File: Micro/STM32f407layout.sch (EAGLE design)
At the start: 44 parts, among them Q1 ASF, T3 FDN340P, T4 AP1117_LIN_REG

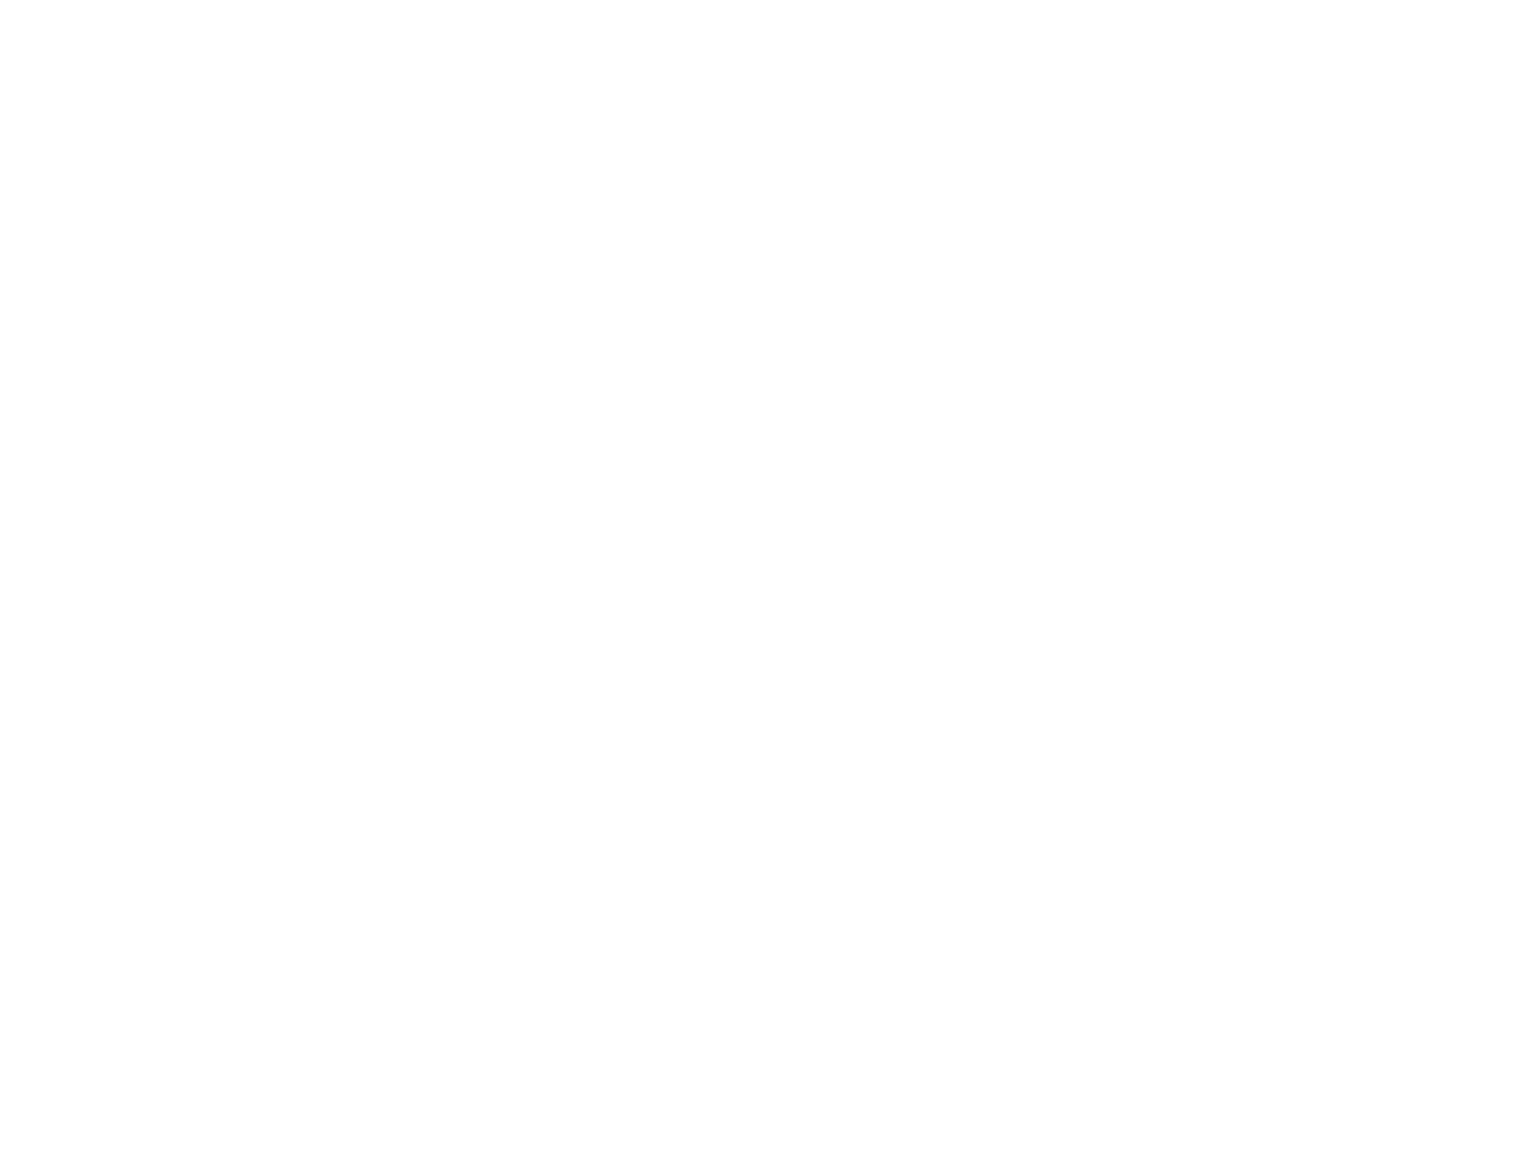
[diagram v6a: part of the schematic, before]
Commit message: Ethernet Addition
I added the ethernet chip and added essential routes, need to do
tolerance checks
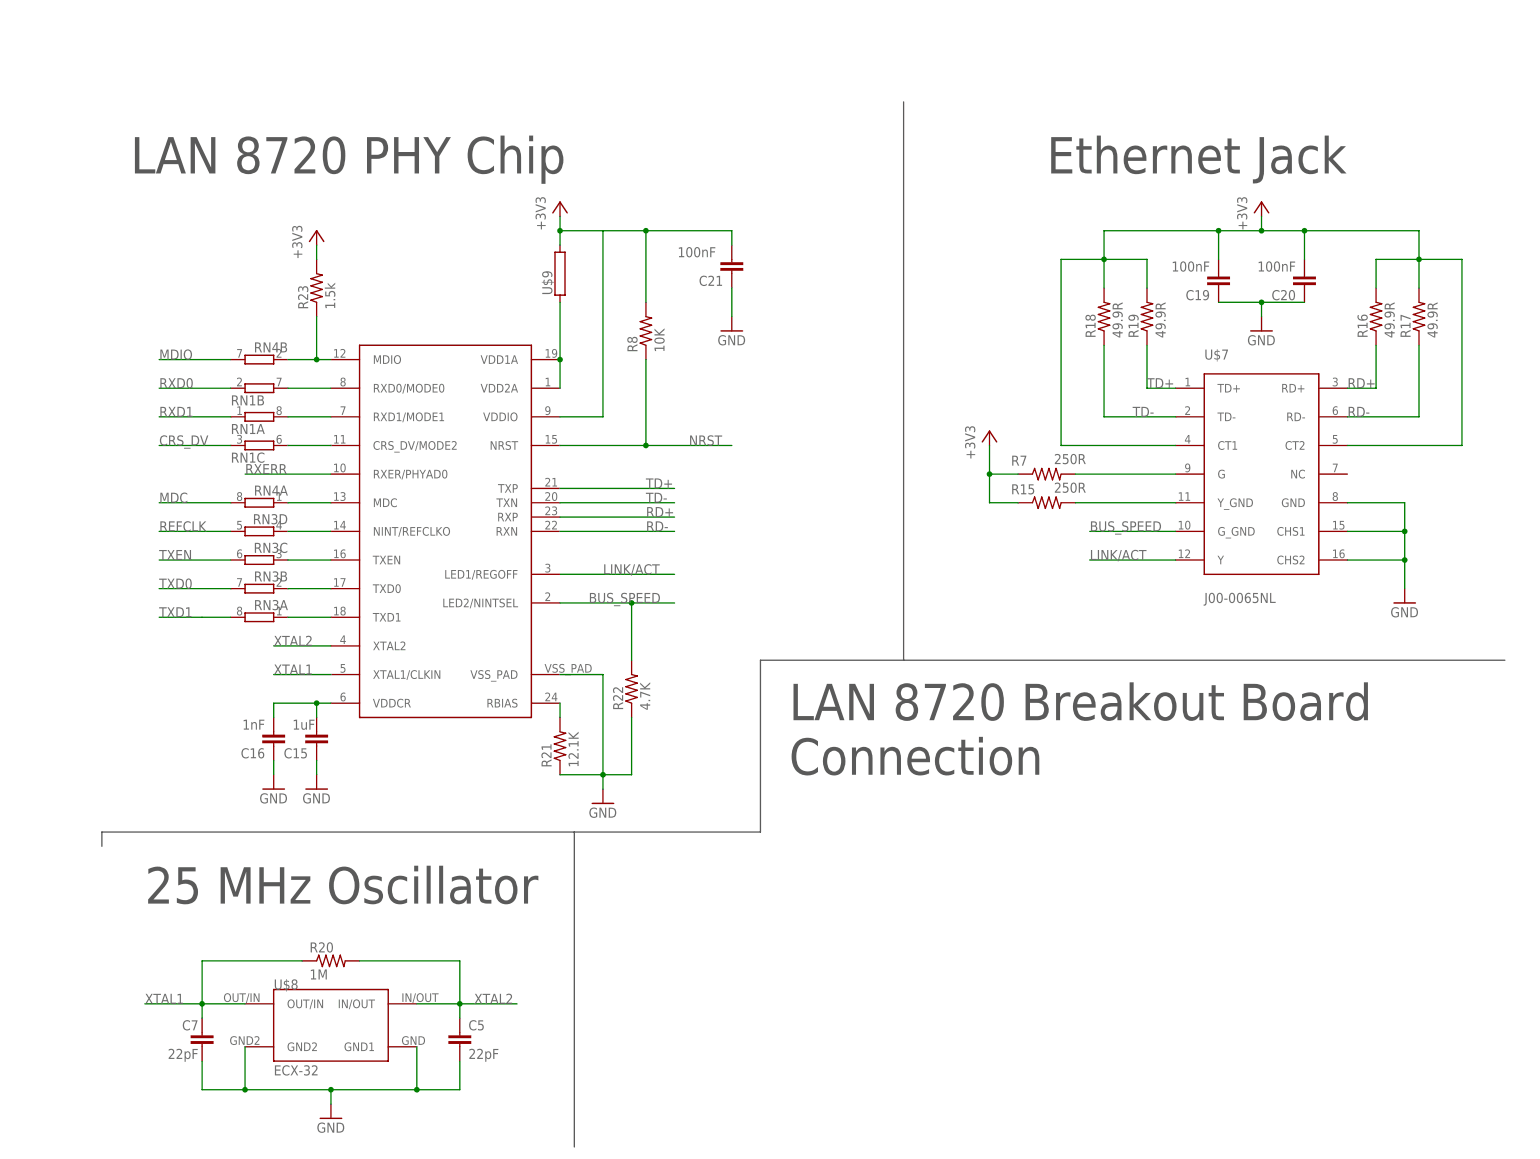
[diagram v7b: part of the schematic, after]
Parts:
- added C15: 1uF, eagle-ltspice:CC0603
- added C16: 1nF, eagle-ltspice:CC0603
- added C19, C20, C21: 100nF, eagle-ltspice:CC0603
- added C5, C7: 22pF, eagle-ltspice:CC0603
- added R15, R7: 250R, resistor:R-US_R0603
- added R16, R17, R18, R19: 49.9R, resistor:R-US_R0603
- added R20: 1M, resistor:R-US_R0603
- added R21: 12.1K, resistor:R-US_R0603
- added R22: 4.7K, resistor:R-US_R0603
- added R23: 1.5k, resistor:R-US_R0603
- added R8: 10K, SparkFun-Passives:RESISTOR0603-RES
- added RN1, RN3, RN4: (no value), resistor-dil:4R-NCAY16
- added U$4: LAN8720LAN8720, EthernetChip:LAN8720LAN8720
- added U$7: J00-0065NL, EthernetChip:J00-0065NL
- added U$8: ECX-32, Other:ECX-32
- added U$9: (no value), EthernetChip:553-2382-1-ND
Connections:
- new net BUS_SPEED: R22.2, U$4.LED2/NINTSEL, U$7.G_GND
- new net GREEN: R7.2, U$7.G
- new net LINK/ACT: U$4.LED1/REGOFF, U$7.Y
- new net MDE: RN4A.1, U$4.MDC
- new net N$13: RN3D.1, U$4.NINT/REFCLKO
- new net N$16: RN3C.1, U$4.TXEN
- new net N$19: RN3B.1, U$4.TXD0
- new net N$20: RN3A.1, U$4.TXD1
- new net N$21: U$4.VDD1A, U$4.VDD2A, U$9.1
- new net N$22: R21.2, U$4.RBIAS
- new net N$23: R23.1, RN4B.1, U$4.MDIO
- new net N$25: RN1B.2, U$4.RXD0/MODE0
- new net N$26: RN1A.2, U$4.RXD1/MODE1
- new net N$6: C15.2, C16.2, U$4.VDDCR
- new net N$9: RN1C.2, U$4.CRS_DV/MODE2
- new net NRST: R8.1, U$4.NRST
- new net RD+: R16.1, U$4.RXP, U$7.RD+
- new net RD-: R17.1, U$4.RXN, U$7.RD-
- new net RXERR: U$4.RXER/PHYAD0
- new net TD+: R19.1, U$4.TXP, U$7.TD+
- new net TD-: R18.1, U$4.TXN, U$7.TD-
- new net XTAL1: C7.1, R20.1, U$4.XTAL1/CLKIN, U$8.OUT/IN
- new net XTAL2: C5.1, R20.2, U$4.XTAL2, U$8.IN/OUT
- new net YELLOW: R15.2, U$7.Y_GND
- net +3V3: now also C19.2, C20.2, C21.2, R15.1, R16.2, R17.2, R18.2, R19.2, R23.2, R7.1, R8.2, U$4.VDDIO, U$7.CT1, U$7.CT2, U$9.2
- net CRS_DV: now also RN1C.1
- net GND: now also C15.1, C16.1, C19.1, C20.1, C21.1, C5.2, C7.2, R21.1, R22.1, U$4.VSS_PAD, U$7.CHS1, U$7.CHS2, U$7.GND, U$8.GND1, U$8.GND2
- net MDC: now also RN4A.2
- net MDIO: now also RN4B.2
- net REFCLK: now also RN3D.2
- net RXD0: now also RN1B.1
- net RXD1: now also RN1A.1
- net TXD0: now also RN3B.2
- net TXD1: now also RN3A.2
- net TXEN: now also RN3C.2
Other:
- note added: "25 MHz Oscillator"
- note added: "Ethernet Jack"
- note added: "LAN 8720 Breakout Board Connection"
- note added: "LAN 8720 PHY Chip"

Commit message: Other Update
Updated power and ground, might need more fixing based on other traces.
need to check if can use different pins for Sonar PWM and DAC, as well
as Servo PWMs.
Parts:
- removed C5, C7: 22pF, eagle-ltspice:CC0603
- removed R20: 1M, resistor:R-US_R0603
- removed U$8: ECX-32, Other:ECX-32
- added C22: 0.01uF, resistor:C-EUC0603
- added Q2: ASV-8, MicroBoard:ASF
- added SV5: (no value), con-lsta:FE07-2
- SV4: device con-lsta:FE07-2 -> con-lsta:FE06-2
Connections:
- net +3V3: now also C22.1, Q2.VCC, SV5.1, SV5.2; no longer SV4.2, SV4.5
- net +5V: now also SV4.1
- net ALT_CAMERA_SERVO_MOTOR_PWM: now also SV4.12
- net CANH1: now also SV4.3
- net CANL1: now also SV4.4
- net CRS_DV: now also SV5.7; no longer SV4.7
- net GND: now also C22.2, Q2.GND, SV4.2, SV5.3, SV5.4; no longer C5.2, C7.2, SV4.3, SV4.4, U$8.GND1, U$8.GND2
- net I2C1_SCL: now also SV4.5
- net I2C1_SDA: now also SV4.6
- net I2C3_SCL: now also SV4.9
- net I2C3_SDA: now also SV4.10
- net MAIN_CAMERA_SERVO_MOTOR_PWM: now also SV4.11
- net MDC: now also SV5.5; no longer SV4.1
- net MDIO: now also SV5.6; no longer SV4.6
- net REFCLK: now also SV5.8; no longer SV4.8
- net RXD0: now also SV5.10; no longer SV4.10
- net RXD1: now also SV5.9; no longer SV4.9
- net SONAR_DAC: now also SV4.8
- net SONAR_PWM: now also SV4.7
- net TXD0: now also SV5.11; no longer SV4.14
- net TXD1: now also SV5.14; no longer SV4.11
- net TXEN: now also SV5.12; no longer SV4.12
- net XTAL1: now also Q2.FO; no longer C7.1, R20.1, U$8.OUT/IN
- net XTAL2: no longer C5.1, R20.2, U$8.IN/OUT
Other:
- note added: "50 MHz Oscillator"
- note removed: "25 MHz Oscillator"
